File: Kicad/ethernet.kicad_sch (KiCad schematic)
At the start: 27 parts, among them J1001 RJ45 MagJack, U1001 ENC424J600, Y1001 25M

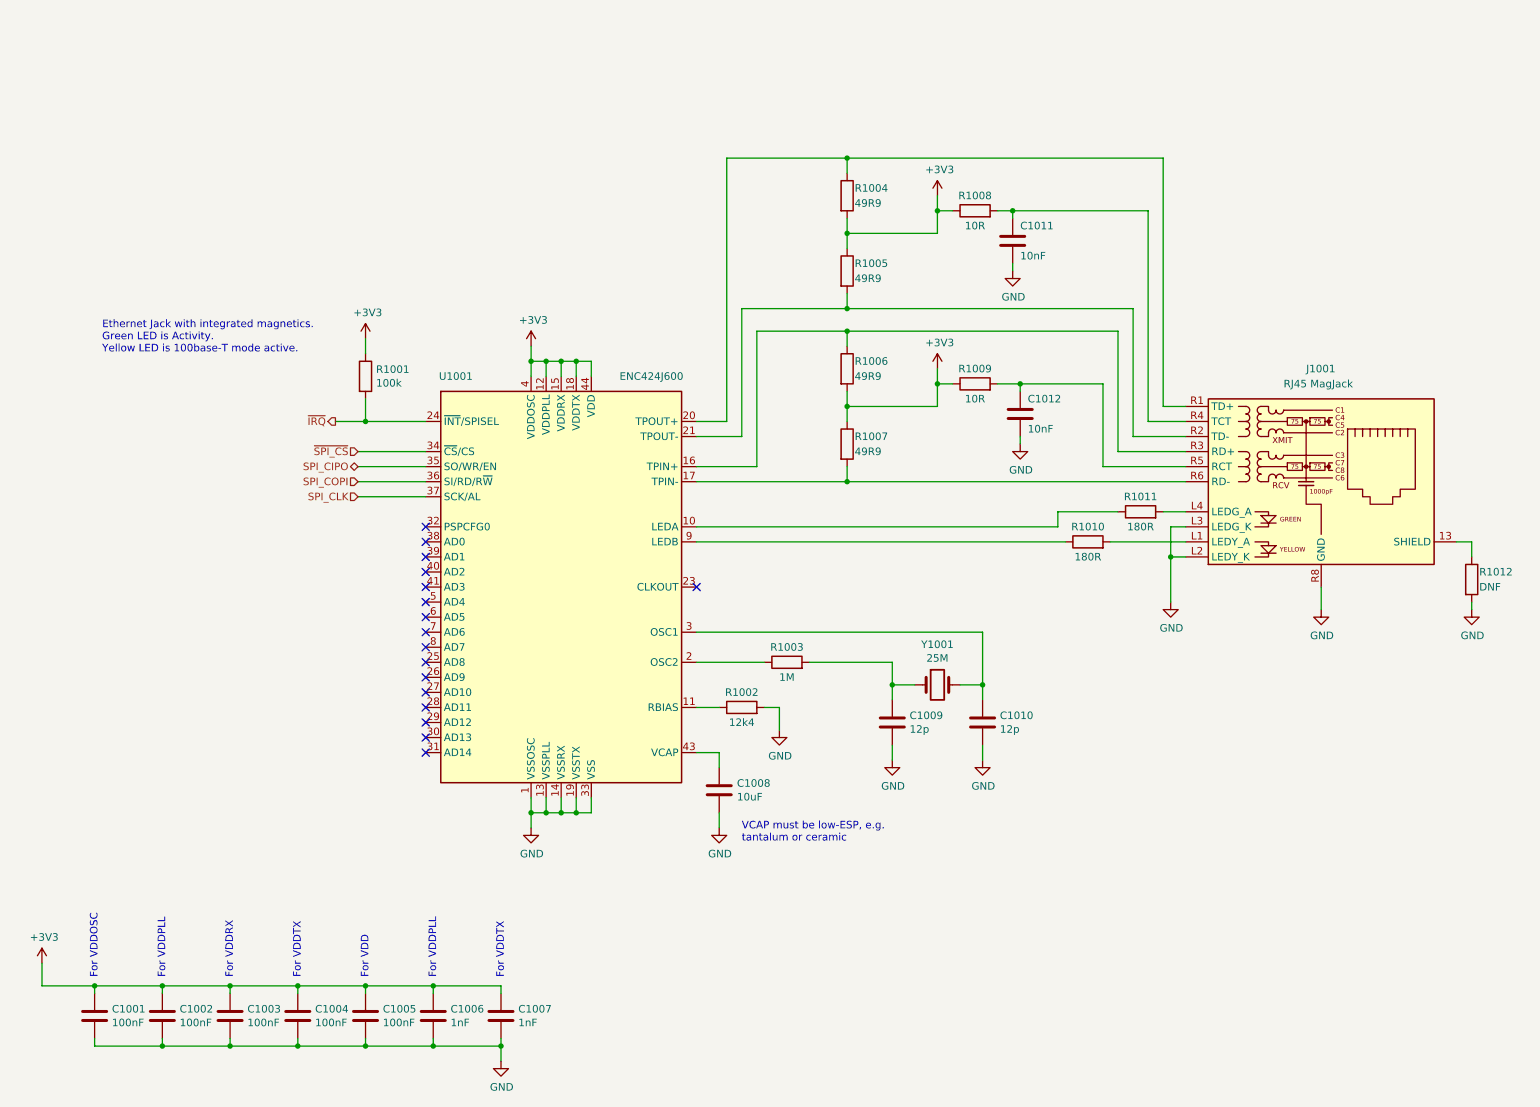
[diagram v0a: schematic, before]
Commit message: Update schematic files to Kicad 6.
Had to fix some symbols which didn't have perfect matches in K6.
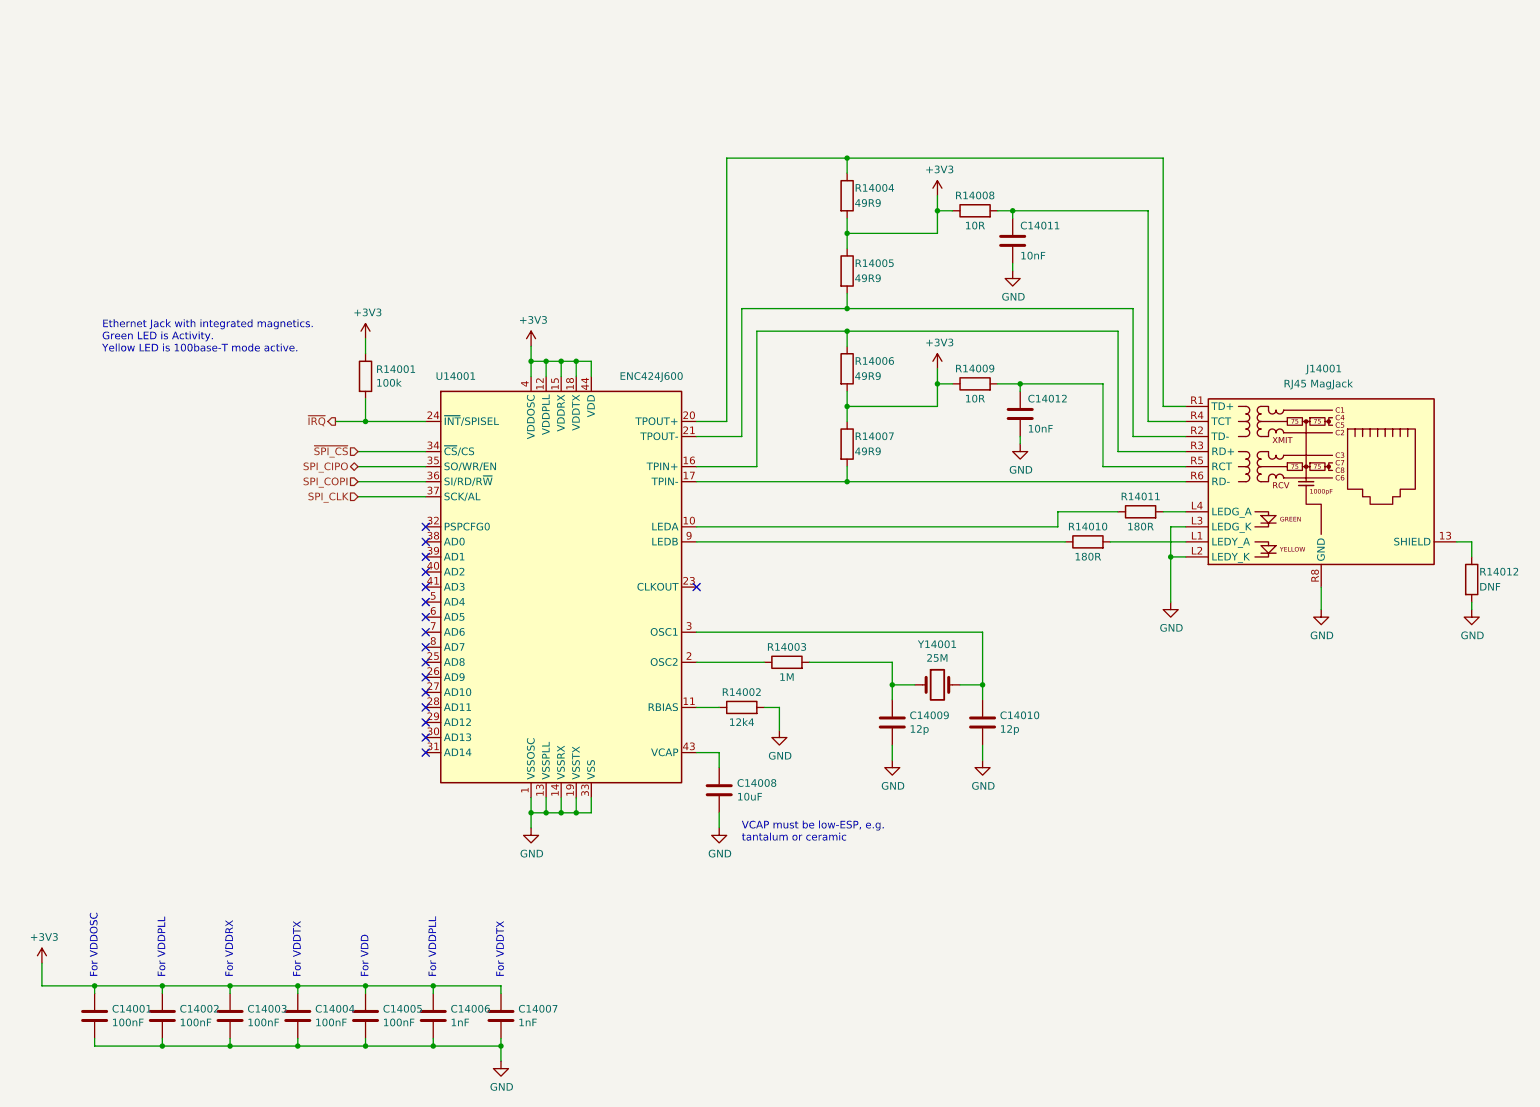
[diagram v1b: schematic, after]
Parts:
- renumbered C1001 to C14001, C1002 to C14002, C1003 to C14003, C1004 to C14004, C1005 to C14005, C1006 to C14006, C1007 to C14007, C1008 to C14008, C1009 to C14009, C1010 to C14010, C1011 to C14011, C1012 to C14012, J1001 to J14001, R1001 to R14001, R1002 to R14002, R1003 to R14003, R1004 to R14004, R1005 to R14005, R1006 to R14006, R1007 to R14007, R1008 to R14008, R1009 to R14009, R1010 to R14010, R1011 to R14011, R1012 to R14012, U1001 to U14001, Y1001 to Y14001

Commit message: Set missing footprints and update PCB
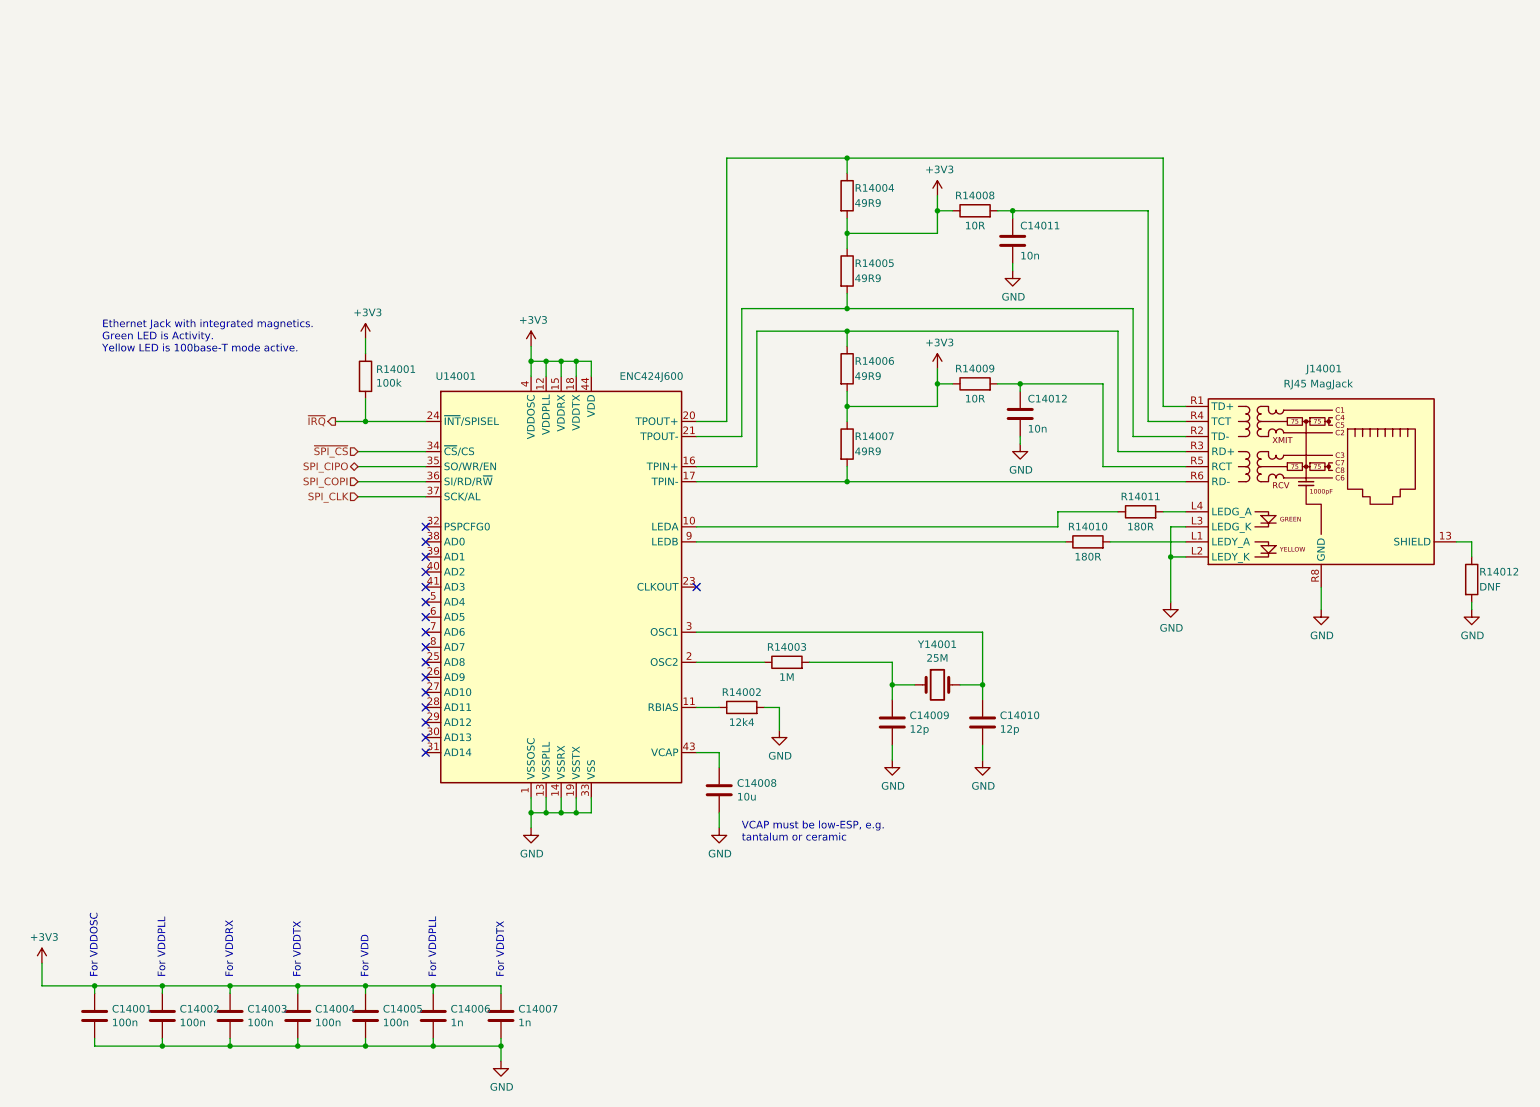
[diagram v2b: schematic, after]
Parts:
- C14001, C14002, C14003, C14004, C14005: value 100nF -> 100n; Digikey BC1150CT-ND -> (none); JLCPCB Collection (none) -> Basic; LCSC Part# (none) -> C49678; MPN CPL-CAP-X7R-0805-100NF-50V -> CC0805KRX7R9BB104
- C14006, C14007: value 1nF -> 1n
- C14008: value 10uF -> 10u; Digikey 1276-6455-1-ND -> (none); MPN CPL-CAP-X5R-0805-10UF-16V -> (none); Manufacturer Samsung -> (none)
- C14011, C14012: value 10nF -> 10n; Digikey 1276-1249-1-ND -> (none); JLCPCB Collection (none) -> Basic; LCSC Part# (none) -> C1710
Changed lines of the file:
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@@
       (effects (font (size 1.27 1.27)) (justify left))
     )
-    (property "Value" "100nF" (id 1) (at 76.581 185.293 0)
+    (property "Value" "100n" (id 1) (at 76.581 185.293 0)
       (effects (font (size 1.27 1.27)) (justify left))
     )
@@
       (effects (font (size 1.27 1.27)) hide)
     )
-    (property "Digikey" "BC1150CT-ND" (id 5) (at 73.66 184.15 0)
-      (effects (font (size 1.27 1.27)) hide)
-    )
-    (property "MPN" "CPL-CAP-X7R-0805-100NF-50V" (id 6) (at 73.66 184.15 0)
+    (property "Digikey" "~" (id 5) (at 73.66 184.15 0)
+      (effects (font (size 1.27 1.27)) hide)
+    )
+    (property "MPN" "CC0805KRX7R9BB104" (id 6) (at 73.66 184.15 0)
       (effects (font (size 1.27 1.27)) hide)
     )
@@
       (effects (font (size 1.27 1.27)) hide)
     )
+    (property "JLCPCB Collection" "Basic" (id 11) (at 73.66 184.15 0)
+      (effects (font (size 1.27 1.27)) hide)
+    )
+    (property "LCSC Part#" "C49678" (id 12) (at 73.66 184.15 0)
+      (effects (font (size 1.27 1.27)) hide)
+    )
     (pin "1")
     (pin "2")
@@
       (effects (font (size 1.27 1.27)) (justify left))
     )
-    (property "Value" "10uF" (id 1) (at 136.3472 147.193 0)
+    (property "Value" "10u" (id 1) (at 136.3472 147.193 0)
       (effects (font (size 1.27 1.27)) (justify left))
     )
@@
       (effects (font (size 1.27 1.27)) hide)
     )
-    (property "Digikey" "1276-6455-1-ND" (id 5) (at 133.35 146.05 0)
-      (effects (font (size 1.27 1.27)) hide)
-    )
-    (property "MPN" "CPL-CAP-X5R-0805-10UF-16V" (id 6) (at 133.35 146.05 0)
-      (effects (font (size 1.27 1.27)) hide)
-    )
-    (property "Manufacturer" "Samsung" (id 7) (at 133.35 146.05 0)
+    (property "Digikey" "" (id 5) (at 133.35 146.05 0)
+      (effects (font (size 1.27 1.27)) hide)
+    )
+    (property "MPN" "" (id 6) (at 133.35 146.05 0)
+      (effects (font (size 1.27 1.27)) hide)
+    )
+    (property "Manufacturer" "" (id 7) (at 133.35 146.05 0)
       (effects (font (size 1.27 1.27)) hide)
     )
@@
       (effects (font (size 1.27 1.27)) (justify left))
     )
-    (property "Value" "100nF" (id 1) (at 65.151 185.293 0)
+    (property "Value" "100n" (id 1) (at 65.151 185.293 0)
       (effects (font (size 1.27 1.27)) (justify left))
     )
@@
       (effects (font (size 1.27 1.27)) hide)
     )
-    (property "Digikey" "BC1150CT-ND" (id 5) (at 62.23 184.15 0)
-      (effects (font (size 1.27 1.27)) hide)
-    )
-    (property "MPN" "CPL-CAP-X7R-0805-100NF-50V" (id 6) (at 62.23 184.15 0)
+    (property "Digikey" "~" (id 5) (at 62.23 184.15 0)
+      (effects (font (size 1.27 1.27)) hide)
+    )
+    (property "MPN" "CC0805KRX7R9BB104" (id 6) (at 62.23 184.15 0)
       (effects (font (size 1.27 1.27)) hide)
     )
@@
       (effects (font (size 1.27 1.27)) hide)
     )
+    (property "JLCPCB Collection" "Basic" (id 11) (at 62.23 184.15 0)
+      (effects (font (size 1.27 1.27)) hide)
+    )
+    (property "LCSC Part#" "C49678" (id 12) (at 62.23 184.15 0)
+      (effects (font (size 1.27 1.27)) hide)
+    )
     (pin "1")
     (pin "2")
@@
       (effects (font (size 1.27 1.27)) (justify left))
     )
-    (property "Value" "100nF" (id 1) (at 53.721 185.293 0)
+    (property "Value" "100n" (id 1) (at 53.721 185.293 0)
       (effects (font (size 1.27 1.27)) (justify left))
     )
@@
       (effects (font (size 1.27 1.27)) hide)
     )
-    (property "Digikey" "BC1150CT-ND" (id 5) (at 50.8 184.15 0)
-      (effects (font (size 1.27 1.27)) hide)
-    )
-    (property "MPN" "CPL-CAP-X7R-0805-100NF-50V" (id 6) (at 50.8 184.15 0)
+    (property "Digikey" "~" (id 5) (at 50.8 184.15 0)
+      (effects (font (size 1.27 1.27)) hide)
+    )
+    (property "MPN" "CC0805KRX7R9BB104" (id 6) (at 50.8 184.15 0)
       (effects (font (size 1.27 1.27)) hide)
     )
@@
       (effects (font (size 1.27 1.27)) hide)
     )
+    (property "JLCPCB Collection" "Basic" (id 11) (at 50.8 184.15 0)
+      (effects (font (size 1.27 1.27)) hide)
+    )
+    (property "LCSC Part#" "C49678" (id 12) (at 50.8 184.15 0)
+      (effects (font (size 1.27 1.27)) hide)
+    )
     (pin "1")
     (pin "2")
@@
       (effects (font (size 1.27 1.27)) (justify left))
     )
-    (property "Value" "100nF" (id 1) (at 42.291 185.293 0)
+    (property "Value" "100n" (id 1) (at 42.291 185.293 0)
       (effects (font (size 1.27 1.27)) (justify left))
     )
@@
       (effects (font (size 1.27 1.27)) hide)
     )
-    (property "Digikey" "BC1150CT-ND" (id 5) (at 39.37 184.15 0)
-      (effects (font (size 1.27 1.27)) hide)
-    )
-    (property "MPN" "CPL-CAP-X7R-0805-100NF-50V" (id 6) (at 39.37 184.15 0)
+    (property "Digikey" "~" (id 5) (at 39.37 184.15 0)
+      (effects (font (size 1.27 1.27)) hide)
+    )
+    (property "MPN" "CC0805KRX7R9BB104" (id 6) (at 39.37 184.15 0)
       (effects (font (size 1.27 1.27)) hide)
     )
@@
       (effects (font (size 1.27 1.27)) hide)
     )
+    (property "JLCPCB Collection" "Basic" (id 11) (at 39.37 184.15 0)
+      (effects (font (size 1.27 1.27)) hide)
+    )
+    (property "LCSC Part#" "C49678" (id 12) (at 39.37 184.15 0)
+      (effects (font (size 1.27 1.27)) hide)
+    )
     (pin "1")
     (pin "2")
@@
       (effects (font (size 1.27 1.27)) (justify left))
     )
-    (property "Value" "100nF" (id 1) (at 30.861 185.293 0)
+    (property "Value" "100n" (id 1) (at 30.861 185.293 0)
       (effects (font (size 1.27 1.27)) (justify left))
     )
@@
       (effects (font (size 1.27 1.27)) hide)
     )
-    (property "Digikey" "BC1150CT-ND" (id 5) (at 27.94 184.15 0)
-      (effects (font (size 1.27 1.27)) hide)
-    )
-    (property "MPN" "CPL-CAP-X7R-0805-100NF-50V" (id 6) (at 27.94 184.15 0)
+    (property "Digikey" "~" (id 5) (at 27.94 184.15 0)
+      (effects (font (size 1.27 1.27)) hide)
+    )
+    (property "MPN" "CC0805KRX7R9BB104" (id 6) (at 27.94 184.15 0)
       (effects (font (size 1.27 1.27)) hide)
     )
@@
     )
     (property "Voltage" "10V" (id 10) (at 27.94 184.15 0)
+      (effects (font (size 1.27 1.27)) hide)
+    )
+    (property "JLCPCB Collection" "Basic" (id 11) (at 27.94 184.15 0)
+      (effects (font (size 1.27 1.27)) hide)
+    )
+    (property "LCSC Part#" "C49678" (id 12) (at 27.94 184.15 0)
       (effects (font (size 1.27 1.27)) hide)
     )
@@
       (effects (font (size 1.27 1.27)) (justify left))
     )
-    (property "Value" "1nF" (id 1) (at 99.441 185.293 0)
+    (property "Value" "1n" (id 1) (at 99.441 185.293 0)
       (effects (font (size 1.27 1.27)) (justify left))
     )
@@
       (effects (font (size 1.27 1.27)) (justify left))
     )
-    (property "Value" "1nF" (id 1) (at 88.011 185.293 0)
+    (property "Value" "1n" (id 1) (at 88.011 185.293 0)
       (effects (font (size 1.27 1.27)) (justify left))
     )
@@
       (effects (font (size 1.27 1.27)) (justify left))
     )
-    (property "Value" "10nF" (id 1) (at 184.15 55.88 0)
+    (property "Value" "10n" (id 1) (at 184.15 55.88 0)
       (effects (font (size 1.27 1.27)) (justify left))
     )
@@
       (effects (font (size 1.27 1.27)) hide)
     )
-    (property "Digikey" "1276-1249-1-ND" (id 5) (at 182.88 53.34 0)
+    (property "Digikey" "~" (id 5) (at 182.88 53.34 0)
       (effects (font (size 1.27 1.27)) hide)
     )
@@
     )
     (property "Voltage" "50V" (id 9) (at 182.88 53.34 0)
+      (effects (font (size 1.27 1.27)) hide)
+    )
+    (property "JLCPCB Collection" "Basic" (id 10) (at 182.88 53.34 0)
+      (effects (font (size 1.27 1.27)) hide)
+    )
+    (property "LCSC Part#" "C1710" (id 11) (at 182.88 53.34 0)
       (effects (font (size 1.27 1.27)) hide)
     )
@@
       (effects (font (size 1.27 1.27)) (justify left))
     )
-    (property "Value" "10nF" (id 1) (at 185.42 85.09 0)
+    (property "Value" "10n" (id 1) (at 185.42 85.09 0)
       (effects (font (size 1.27 1.27)) (justify left))
     )
@@
       (effects (font (size 1.27 1.27)) hide)
     )
-    (property "Digikey" "1276-1249-1-ND" (id 5) (at 184.15 82.55 0)
+    (property "Digikey" "~" (id 5) (at 184.15 82.55 0)
       (effects (font (size 1.27 1.27)) hide)
     )
@@
       (effects (font (size 1.27 1.27)) hide)
     )
+    (property "JLCPCB Collection" "Basic" (id 10) (at 184.15 82.55 0)
+      (effects (font (size 1.27 1.27)) hide)
+    )
+    (property "LCSC Part#" "C1710" (id 11) (at 184.15 82.55 0)
+      (effects (font (size 1.27 1.27)) hide)
+    )
